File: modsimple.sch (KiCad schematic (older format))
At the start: 11 parts, among them J1 MICROUSB, P1 CONN_10, Q2 FDD8870, U1 MAX1555

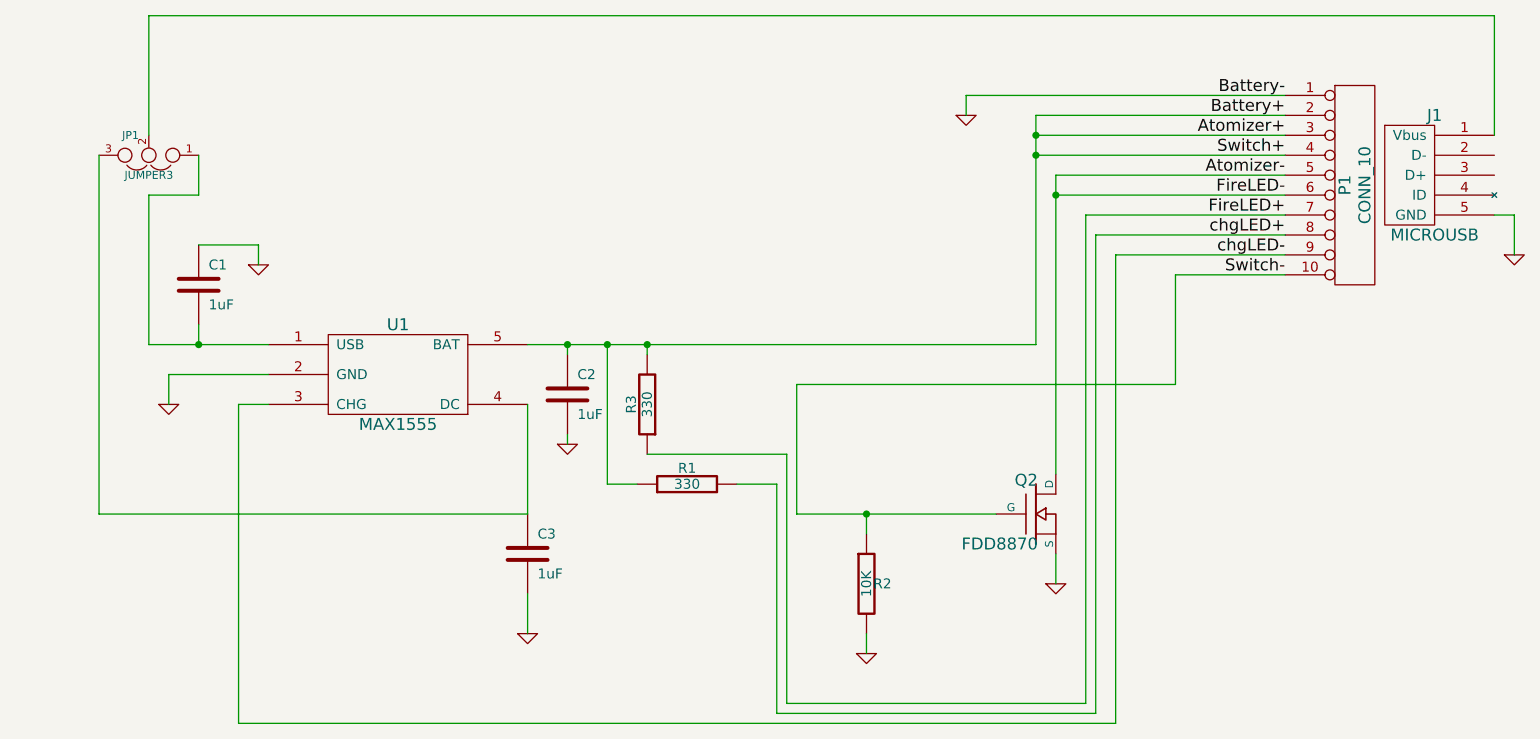
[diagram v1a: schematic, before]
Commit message: Switched to MAX1811
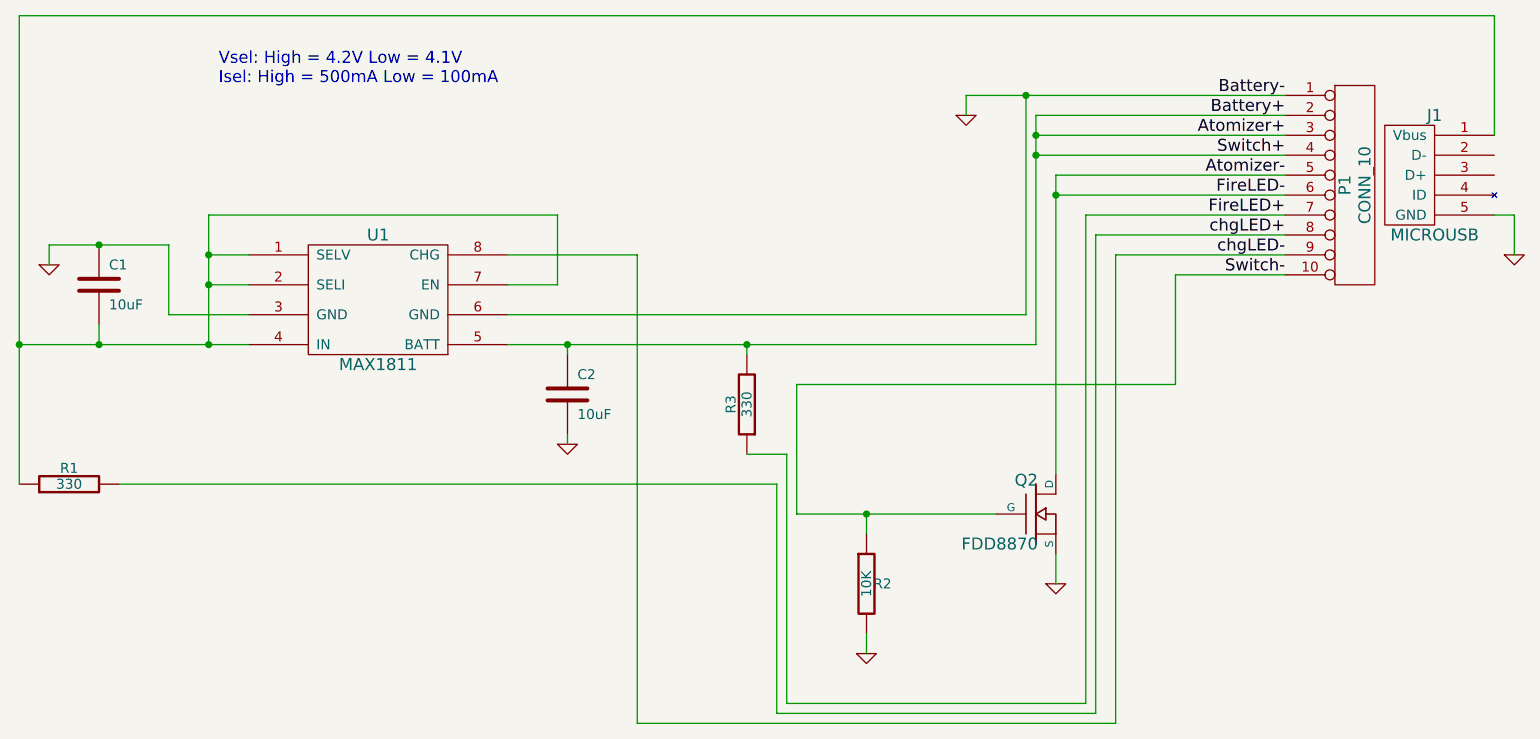
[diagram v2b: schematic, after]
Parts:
- removed C3: 1uF, symbol C
- removed JP1: JUMPER3, symbol JUMPER3
- removed U1: MAX1555, symbol MAX1555
- added U1: MAX1811, symbol MAX1811
- C1, C2: value 1uF -> 10uF
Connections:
- net Atomizer+: now also U1.5 (BATT); no longer R1.1
- net GND: now also U1.3 (GND), U1.6 (GND)
- net chgLED-: now also U1.8 (CHG)
- net at C1.2: now also J1.1 (Vbus), R1.1, U1.1 (SELV), U1.2 (SELI), U1.4 (IN), U1.7 (EN)
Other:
- note added: "Vsel: High = 4.2V Low = 4.1V\nIsel: High = 500mA Low = 100mA"
- moved on the sheet: C1, R1, R3
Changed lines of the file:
@@
-EESchema Schematic File Version 2  date Tue 12 Mar 2013 12:01:35 PM CDT
+EESchema Schematic File Version 2  date Sun 24 Mar 2013 02:18:00 PM CDT
 LIBS:power
 LIBS:device
@@
 Sheet 1 1
 Title ""
-Date "12 mar 2013"
+Date "24 mar 2013"
 Rev ""
 Comp ""
@@
 L R R3
 U 1 1 5133879A
-P 6850 4550
-F 0 "R3" V 6930 4550 50  0000 C CNN
-F 1 "330" V 6850 4550 50  0000 C CNN
-F 2 "" H 6850 4550 60  0001 C CNN
-F 3 "" H 6850 4550 60  0001 C CNN
-	1    6850 4550
+P 7350 4550
+F 0 "R3" V 7430 4550 50  0000 C CNN
+F 1 "330" V 7350 4550 50  0000 C CNN
+F 2 "" H 7350 4550 60  0001 C CNN
+F 3 "" H 7350 4550 60  0001 C CNN
+	1    7350 4550
 	-1   0    0    1
 $EndComp
 $Comp
-L GND #PWR01
-U 1 1 5133869F
-P 6250 5700
-F 0 "#PWR01" H 6250 5700 30  0001 C CNN
-F 1 "GND" H 6250 5630 30  0001 C CNN
-F 2 "" H 6250 5700 60  0001 C CNN
-F 3 "" H 6250 5700 60  0001 C CNN
-	1    6250 5700
-	1    0    0    -1
-$EndComp
-$Comp
-L C C3
-U 1 1 51338696
-P 6250 5300
-F 0 "C3" H 6300 5400 50  0000 L CNN
-F 1 "1uF" H 6300 5200 50  0000 L CNN
-F 2 "" H 6250 5300 60  0001 C CNN
-F 3 "" H 6250 5300 60  0001 C CNN
-	1    6250 5300
-	1    0    0    -1
-$EndComp
-$Comp
-L GND #PWR02
+L GND #PWR3
 U 1 1 513187A3
 P 7950 5800
-F 0 "#PWR02" H 7950 5800 30  0001 C CNN
+F 0 "#PWR3" H 7950 5800 30  0001 C CNN
 F 1 "GND" H 7950 5730 30  0001 C CNN
 F 2 "" H 7950 5800 60  0001 C CNN
@@
 Atomizer-
 $Comp
-L GND #PWR03
+L GND #PWR5
 U 1 1 51302ACE
 P 8900 5450
-F 0 "#PWR03" H 8900 5450 30  0001 C CNN
+F 0 "#PWR5" H 8900 5450 30  0001 C CNN
 F 1 "GND" H 8900 5380 30  0001 C CNN
 F 2 "" H 8900 5450 60  0001 C CNN
@@
 Battery+
 $Comp
-L GND #PWR04
+L GND #PWR6
 U 1 1 512C4AF2
 P 11200 3800
-F 0 "#PWR04" H 11200 3800 30  0001 C CNN
+F 0 "#PWR6" H 11200 3800 30  0001 C CNN
 F 1 "GND" H 11200 3730 30  0001 C CNN
 F 2 "" H 11200 3800 60  0001 C CNN
@@
 $EndComp
 $Comp
-L JUMPER3 JP1
-U 1 1 512B9DDA
-P 4350 3300
-F 0 "JP1" H 4400 3200 40  0000 L CNN
-F 1 "JUMPER3" H 4350 3400 40  0000 C CNN
-F 2 "" H 4350 3300 60  0001 C CNN
-F 3 "" H 4350 3300 60  0001 C CNN
-	1    4350 3300
-	-1   0    0    1
-$EndComp
-$Comp
-L GND #PWR05
+L GND #PWR2
 U 1 1 512B9659
 P 6450 4750
-F 0 "#PWR05" H 6450 4750 30  0001 C CNN
+F 0 "#PWR2" H 6450 4750 30  0001 C CNN
 F 1 "GND" H 6450 4680 30  0001 C CNN
 F 2 "" H 6450 4750 60  0001 C CNN
@@
 P 6450 4500
 F 0 "C2" H 6500 4600 50  0000 L CNN
-F 1 "1uF" H 6500 4400 50  0000 L CNN
+F 1 "10uF" H 6500 4400 50  0000 L CNN
 F 2 "" H 6450 4500 60  0001 C CNN
 F 3 "" H 6450 4500 60  0001 C CNN
@@
 $EndComp
 $Comp
-L GND #PWR06
+L GND #PWR1
 U 1 1 512B9625
-P 4900 3850
-F 0 "#PWR06" H 4900 3850 30  0001 C CNN
-F 1 "GND" H 4900 3780 30  0001 C CNN
-F 2 "" H 4900 3850 60  0001 C CNN
-F 3 "" H 4900 3850 60  0001 C CNN
-	1    4900 3850
+P 3850 3850
+F 0 "#PWR1" H 3850 3850 30  0001 C CNN
+F 1 "GND" H 3850 3780 30  0001 C CNN
+F 2 "" H 3850 3850 60  0001 C CNN
+F 3 "" H 3850 3850 60  0001 C CNN
+	1    3850 3850
 	1    0    0    -1
 $EndComp
@@
 L C C1
 U 1 1 512B9601
-P 4600 3950
-F 0 "C1" H 4650 4050 50  0000 L CNN
-F 1 "1uF" H 4650 3850 50  0000 L CNN
-F 2 "" H 4600 3950 60  0001 C CNN
-F 3 "" H 4600 3950 60  0001 C CNN
-	1    4600 3950
+P 4100 3950
+F 0 "C1" H 4150 4050 50  0000 L CNN
+F 1 "10uF" H 4150 3850 50  0000 L CNN
+F 2 "" H 4100 3950 60  0001 C CNN
+F 3 "" H 4100 3950 60  0001 C CNN
+	1    4100 3950
 	1    0    0    -1
 $EndComp
@@
 L R R1
 U 1 1 512B94C6
-P 7050 4950
-F 0 "R1" V 7130 4950 50  0000 C CNN
-F 1 "330" V 7050 4950 50  0000 C CNN
-F 2 "" H 7050 4950 60  0001 C CNN
-F 3 "" H 7050 4950 60  0001 C CNN
-	1    7050 4950
+P 3950 4950
+F 0 "R1" V 4030 4950 50  0000 C CNN
+F 1 "330" V 3950 4950 50  0000 C CNN
+F 2 "" H 3950 4950 60  0001 C CNN
+F 3 "" H 3950 4950 60  0001 C CNN
+	1    3950 4950
 	0    -1   -1   0
-$EndComp
-$Comp
-L GND #PWR07
-U 1 1 512B93CD
-P 4450 4550
-F 0 "#PWR07" H 4450 4550 30  0001 C CNN
-F 1 "GND" H 4450 4480 30  0001 C CNN
-F 2 "" H 4450 4550 60  0001 C CNN
-F 3 "" H 4450 4550 60  0001 C CNN
-	1    4450 4550
-	1    0    0    -1
 $EndComp
 $Comp
@@
 $EndComp
 $Comp
-L MAX1555 U1
-U 1 1 512B0BCD
-P 5600 4650
-F 0 "U1" H 5600 5150 60  0000 C CNN
-F 1 "MAX1555" H 5600 4650 60  0000 C CNN
-F 2 "" H 5600 4650 60  0001 C CNN
-F 3 "" H 5600 4650 60  0001 C CNN
-	1    5600 4650
-	1    0    0    -1
-$EndComp
-$Comp
-L GND #PWR08
+L GND #PWR4
 U 1 1 512AF9E3
 P 8450 3100
-F 0 "#PWR08" H 8450 3100 30  0001 C CNN
+F 0 "#PWR4" H 8450 3100 30  0001 C CNN
 F 1 "GND" H 8450 3030 30  0001 C CNN
 F 2 "" H 8450 3100 60  0001 C CNN
@@
 Text Label 10050 3500 2    60   ~ 0
 FireLED-
+$Comp
+L MAX1811 U1
+U 1 1 514F4034
+P 5500 4350
+F 0 "U1" H 5500 5000 60  0000 C CNN
+F 1 "MAX1811" H 5500 4350 60  0000 C CNN
+F 2 "" H 5500 4350 60  0000 C CNN
+F 3 "" H 5500 4350 60  0000 C CNN
+	1    5500 4350
+	1    0    0    -1
+$EndComp
 Wire Wire Line
 	8450 3100 8450 3000
@@
 Wire Wire Line
 	10050 3100 8800 3100
-Connection ~ 6850 4250
-Wire Wire Line
-	6850 4250 6850 4300
+Connection ~ 7350 4250
+Wire Wire Line
+	7350 4250 7350 4300
 Wire Wire Line
 	7600 5100 8600 5100
 Wire Wire Line
-	8800 4250 6250 4250
+	8800 4250 6150 4250
 Wire Wire Line
 	8800 3100 8800 4250
 Wire Wire Line
-	4350 2600 11100 2600
-Wire Wire Line
-	4350 2600 4350 3200
+	3700 2600 11100 2600
 Connection ~ 7950 5100
 Wire Wire Line
@@
 	8900 5300 8900 5450
 Wire Wire Line
-	6250 4550 6250 5100
-Wire Wire Line
-	6250 5100 4100 5100
-Wire Wire Line
-	4100 5100 4100 3300
-Wire Wire Line
 	6450 4700 6450 4750
-Connection ~ 4600 4250
-Wire Wire Line
-	4600 4150 4600 4250
-Wire Wire Line
-	4350 4250 4950 4250
+Wire Wire Line
+	4100 4150 4100 4250
+Wire Wire Line
+	3700 4250 4850 4250
 Wire Wire Line
 	11100 2600 11100 3200
-Connection ~ 6650 4250
-Wire Wire Line
-	4950 4400 4450 4400
-Wire Wire Line
-	4450 4400 4450 4550
-Wire Wire Line
-	4600 3750 4900 3750
-Wire Wire Line
-	4900 3750 4900 3850
-Wire Wire Line
-	6450 4300 6450 4250
+Wire Wire Line
+	6450 4250 6450 4300
 Connection ~ 6450 4250
 Wire Wire Line
-	6650 4250 6650 4950
-Wire Wire Line
-	4600 3300 4600 3500
-Wire Wire Line
-	4600 3500 4350 3500
-Wire Wire Line
-	4350 3500 4350 4250
+	3700 2600 3700 4950
 Wire Wire Line
 	11100 3600 11200 3600
@@
 	8800 3200 10050 3200
 Connection ~ 8800 3200
-Wire Wire Line
-	6250 5500 6250 5700
 Connection ~ 8800 3300
 Wire Wire Line
-	6650 4950 6800 4950
-Wire Wire Line
-	6850 4800 7550 4800
+	7350 4800 7550 4800
 Wire Wire Line
 	7550 4800 7550 6050
@@
 	9050 3600 10050 3600
 Wire Wire Line
-	7300 4950 7500 4950
+	4200 4950 7500 4950
 Wire Wire Line
 	7500 4950 7500 6100
@@
 Wire Wire Line
 	9200 3800 9200 6150
-Wire Wire Line
-	9200 6150 4800 6150
-Wire Wire Line
-	4800 6150 4800 4550
-Wire Wire Line
-	4800 4550 4950 4550
 Wire Wire Line
 	10050 3300 8800 3300
@@
 	10050 3500 8900 3500
 Connection ~ 8900 3500
+Wire Wire Line
+	4450 3750 4450 4100
+Wire Wire Line
+	4450 4100 4850 4100
+Connection ~ 4100 4250
+Wire Wire Line
+	3850 3750 4450 3750
+Connection ~ 4100 3750
+Wire Wire Line
+	6150 4100 8750 4100
+Wire Wire Line
+	8750 4100 8750 3000
+Connection ~ 8750 3000
+Connection ~ 3700 4250
+Wire Wire Line
+	4650 3950 4850 3950
+Wire Wire Line
+	9200 6150 6800 6150
+Wire Wire Line
+	6800 6150 6800 3800
+Wire Wire Line
+	6800 3800 6150 3800
+Text Notes 4700 2950 0    60   ~ 0
+Vsel: High = 4.2V Low = 4.1V\nIsel: High = 500mA Low = 100mA
+Wire Wire Line
+	3850 3750 3850 3850
+Wire Wire Line
+	4850 3800 4650 3800
+Wire Wire Line
+	4650 3600 4650 4250
+Connection ~ 4650 4250
+Connection ~ 4650 3950
+Wire Wire Line
+	6150 3950 6400 3950
+Wire Wire Line
+	6400 3950 6400 3600
+Wire Wire Line
+	6400 3600 4650 3600
+Connection ~ 4650 3800
 $EndSCHEMATC
